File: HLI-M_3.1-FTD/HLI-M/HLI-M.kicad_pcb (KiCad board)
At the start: 2 copper layers, 125.2 x 86.1 mm, 122 parts, among them CON1 , CON2 USB_B, CON3 , CON4 Con_ADAPTER, CON5 Con_MULTLINKER, CON6 Conn_01x15, CON7 Conn_01x09, CON8 CR123A, Q1 DMP3068L-7, Q2 BC817, Q3 BC817, Q4 DMP2305, Q5 DMP2305, Q6 DMP2305, Q7 DMP2305, U1 PIC24HJ64GP206, U10 ULN2003, U11 ULN2003, U12 ULN2003, U2 FM25V10, U2-A DFN-8-1EP_6x5mm_P1.27mm_EP2x2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, U3 MAX3232, U4 ATSHA204A-SSHDA-B, U5 24AA02-OT, U5-A SOIC-8_3.9x4.9mm_P1.27mm, U6 LM3658SD, U7 TPS7A0533PDBV, U8 TPS7A0533PDBV, U9 FT232RL, Y1 Crystal_32KHz, Y2 Crystal_20MHz

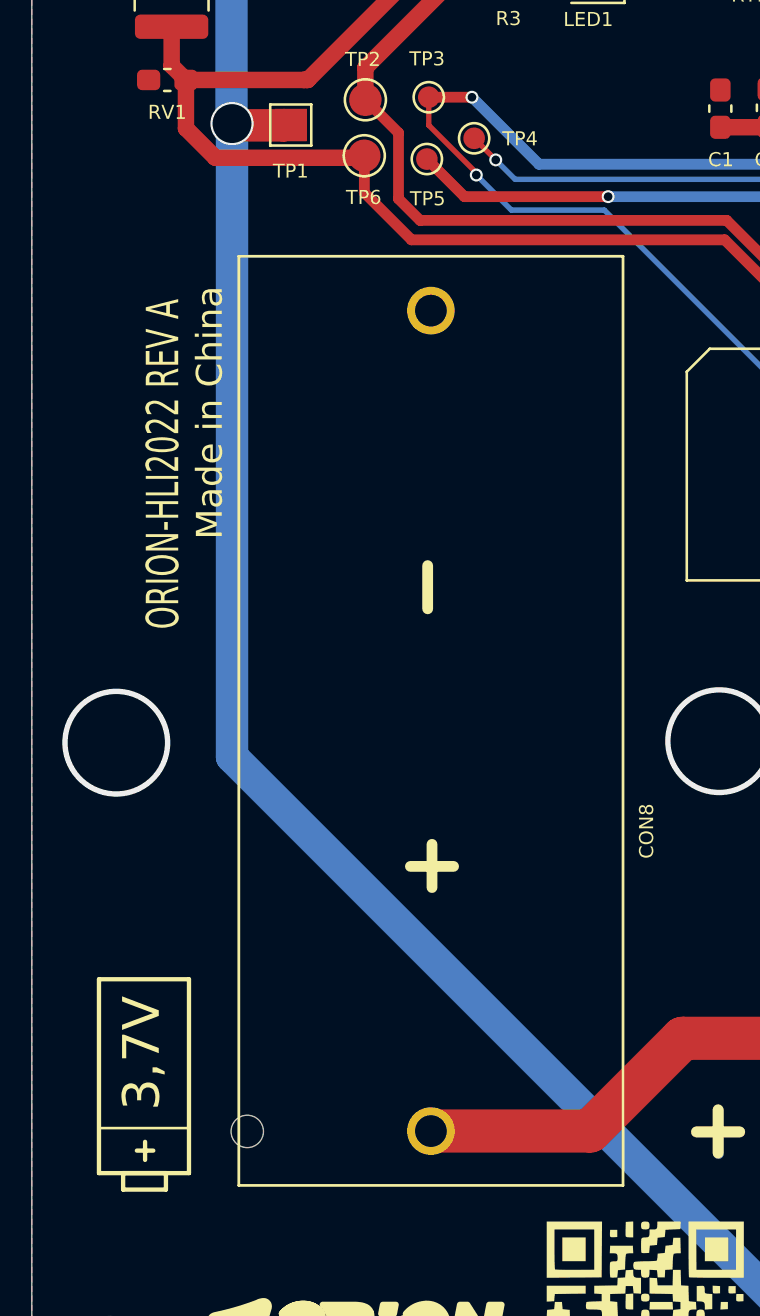
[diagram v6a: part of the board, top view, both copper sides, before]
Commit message: atualização serigrafia e conector bateria
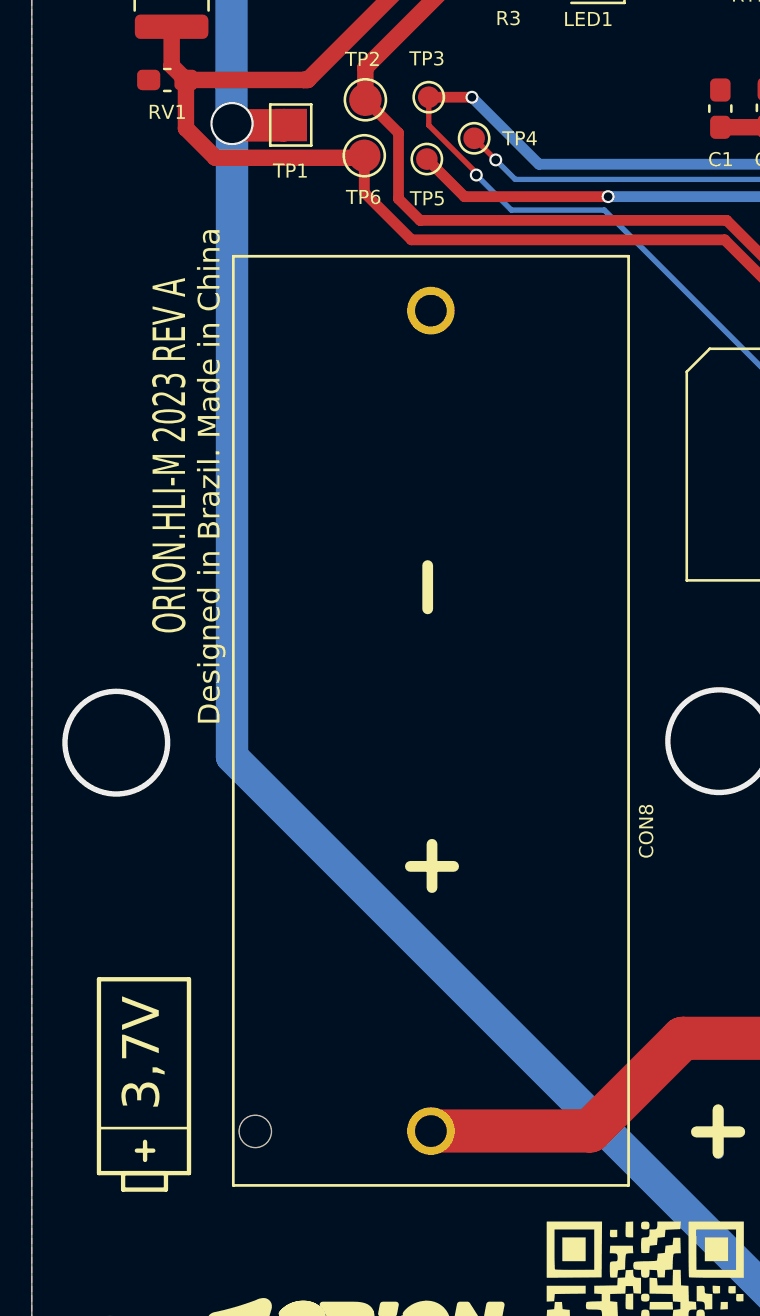
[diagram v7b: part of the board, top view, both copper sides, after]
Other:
- board text added: "Designed in Brazil. Made in China"
- board text added: "ORION.HLI-M 2023 REV A"
- board text removed: "Made in China"
- board text removed: "ORION-HLI2022 REV A"
